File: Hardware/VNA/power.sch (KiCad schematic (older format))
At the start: 40 parts, among them Q1 RE1C002UN, U4 LP5912, U5 LP5912, U6 MIC5366-1.8

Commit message: first day of layout / routing done
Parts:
- F1: footprint VNA_Footprints:Fuse_1206_3216Metric -> VNA_Footprints:Fuse_0805_2012Metric
- Q1: footprint Package_TO_SOT_SMD:SOT-89-3 -> Package_TO_SOT_SMD:SOT-416
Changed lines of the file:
@@
 	5150 3950 5150 3800
 Connection ~ 4950 3950
-Text Notes 4000 3550 0    100  ~ 6
+Text Notes 4000 3550 0    100  ~ 20
 1V8 LDO\n
 Wire Wire Line
@@
 	1    0    0    -1
 $EndComp
-Text Notes 1300 2150 0    100  ~ 6
+Text Notes 1300 2150 0    100  ~ 20
 5V (Filtered)
-Text HLabel 3350 3800 1    49   Input ~ 6
+Text HLabel 3350 3800 1    49   Input ~ 10
 3V3A
-Text HLabel 5150 3800 1    49   Input ~ 6
+Text HLabel 5150 3800 1    49   Input ~ 10
 1V8
-Text HLabel 2550 2400 1    49   Input ~ 6
+Text HLabel 2550 2400 1    49   Input ~ 10
 5V0
 Wire Wire Line
@@
 	1    0    0    -1
 $EndComp
-Text Notes 2250 3600 2    100  ~ 6
+Text Notes 2250 3600 2    100  ~ 20
 3V3A LDO
 Wire Wire Line
@@
 Wire Wire Line
 	2550 3950 2850 3950
-Text HLabel 2850 3850 1    49   Input ~ 6
+Text HLabel 2850 3850 1    49   Input ~ 10
 3V3A
 Connection ~ 2550 3950
@@
 Wire Wire Line
 	4950 2500 5250 2500
-Text HLabel 5250 2400 1    49   Input ~ 6
+Text HLabel 5250 2400 1    49   Input ~ 10
 3V3
 Connection ~ 4950 2500
@@
 $EndComp
 Connection ~ 3750 2500
-Text Notes 4600 2200 2    100  ~ 6
+Text Notes 4600 2200 2    100  ~ 20
 3V3 LDO
 $Comp
@@
 F 0 "F1" V 1700 1400 50  0000 C CNN
 F 1 "500mA Polyfuse" V 1900 1400 50  0000 C CNN
-F 2 "VNA_Footprints:Fuse_1206_3216Metric" H 1850 1200 50  0001 L CNN
+F 2 "VNA_Footprints:Fuse_0805_2012Metric" H 1850 1200 50  0001 L CNN
 F 3 "~" H 1800 1400 50  0001 C CNN
 	1    1800 1400
 	0    1    1    0
 $EndComp
-Text HLabel 1250 1400 0    49   Input ~ 6
+Text HLabel 1250 1400 0    49   Input ~ 10
 VBUS
 Wire Wire Line
 	1900 1400 2200 1400
-Text Label 2300 1400 0    50   ~ 6
+Text Label 2300 1400 0    50   ~ 10
 VIN
-Text Label 1050 2400 1    50   ~ 6
+Text Label 1050 2400 1    50   ~ 10
 VIN
-Text Label 3350 2400 1    50   ~ 6
+Text Label 3350 2400 1    50   ~ 10
 VIN
-Text Label 1100 3850 1    50   ~ 6
+Text Label 1100 3850 1    50   ~ 10
 VIN
-Text Notes 1200 1150 0    100  ~ 6
+Text Notes 1200 1150 0    100  ~ 20
 Input Protection
 Wire Wire Line
@@
 F 0 "Q1" H 6706 3546 50  0000 L CNN
 F 1 "RE1C002UN" H 6706 3455 50  0000 L CNN
-F 2 "Package_TO_SOT_SMD:SOT-89-3" H 6700 3600 50  0001 C CNN
+F 2 "Package_TO_SOT_SMD:SOT-416" H 6700 3600 50  0001 C CNN
 F 3 "~" H 6500 3500 50  0001 C CNN
 	1    6500 3500
@@
 Wire Wire Line
 	6600 2600 6600 2550
-Text HLabel 6600 2550 1    50   Input ~ 6
+Text HLabel 6600 2550 1    50   Input ~ 10
 3V3A
-Text HLabel 6150 3500 0    50   Input ~ 6
+Text HLabel 6150 3500 0    50   Input ~ 10
 1V8
 Wire Wire Line
@@
 	1    0    0    -1
 $EndComp
-Text Notes 6800 2200 0    100  ~ 6
+Text Notes 6800 2200 0    100  ~ 20
 Voltage Rail LEDs
 Wire Wire Line
 	7250 2600 7250 2550
-Text HLabel 7250 2550 1    50   Input ~ 6
+Text HLabel 7250 2550 1    50   Input ~ 10
 3V3A
 Wire Wire Line
@@
 Wire Wire Line
 	7650 2600 7650 2550
-Text HLabel 7650 2550 1    50   Input ~ 6
+Text HLabel 7650 2550 1    50   Input ~ 10
 3V3
 Wire Wire Line
@@
 Wire Wire Line
 	8050 2600 8050 2550
-Text HLabel 8050 2550 1    50   Input ~ 6
+Text HLabel 8050 2550 1    50   Input ~ 10
 5V0
 Wire Wire Line
@@
 	1    0    0    -1
 $EndComp
-Text HLabel 8400 2550 1    49   Input ~ 6
+Text HLabel 8400 2550 1    49   Input ~ 10
 VBUS
 Connection ~ 5150 3950
@@
 	1    0    0    -1
 $EndComp
-Text Notes 9150 2200 0    100  ~ 6
+Text Notes 9150 2200 0    100  ~ 20
 Ground Test Points
 $Comp

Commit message: no unrouted nets!
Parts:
- Q1: footprint Package_TO_SOT_SMD:SOT-416 -> VNA_Footprints:SOT-416
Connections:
- net GND: no longer U5.3 (PG)
- no-connect marks 1 -> 2
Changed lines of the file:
@@
 $EndComp
-Wire Wire Line
-	4550 2700 4600 2700
-Wire Wire Line
-	4600 2700 4600 2800
 Wire Wire Line
 	4550 3000 4600 3000
@@
 Wire Wire Line
 	4550 2800 4600 2800
-Connection ~ 4600 2800
 Wire Wire Line
 	4600 2800 4600 2900
@@
 F 0 "Q1" H 6706 3546 50  0000 L CNN
 F 1 "RE1C002UN" H 6706 3455 50  0000 L CNN
-F 2 "Package_TO_SOT_SMD:SOT-416" H 6700 3600 50  0001 C CNN
+F 2 "VNA_Footprints:SOT-416" H 6700 3600 50  0001 C CNN
 F 3 "~" H 6500 3500 50  0001 C CNN
 	1    6500 3500
@@
 Wire Wire Line
 	3750 2500 3950 2500
+NoConn ~ 4550 2700
 $EndSCHEMATC

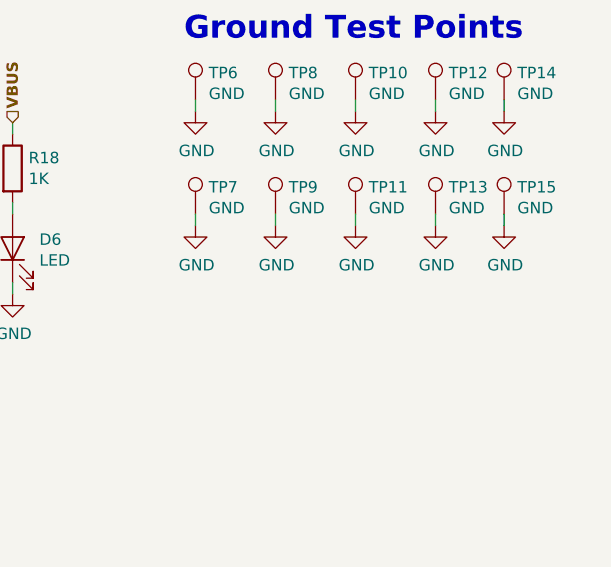
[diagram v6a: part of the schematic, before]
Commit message: Layout done, front and rear panels designed
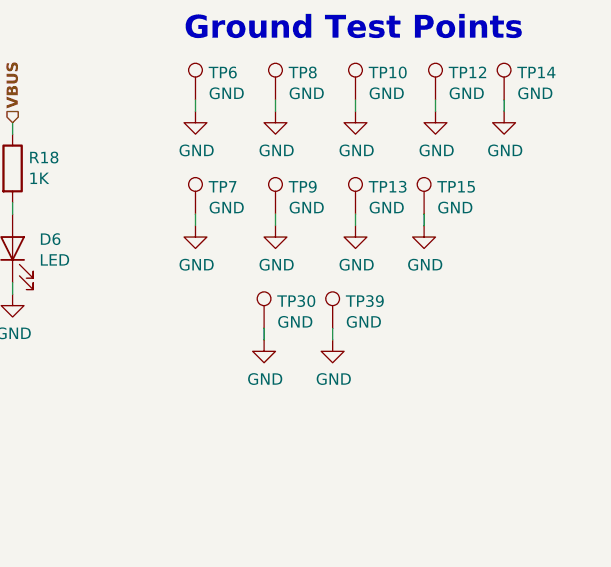
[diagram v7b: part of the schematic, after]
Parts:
- removed TP11: GND, VNA_Footprints:S1751-46_smdTestPoint, symbol Connector:TestPoint
- added TP30, TP39: GND, TestPoint:TestPoint_THTPad_D2.0mm_Drill1.0mm, symbol Connector:TestPoint
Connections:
- net GND: now also TP30.1, TP39.1
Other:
- moved on the sheet: TP13, TP15
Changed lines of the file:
@@
 $EndComp
 $Comp
-L Connector:TestPoint TP11
-U 1 1 5D0E22BA
+L Connector:TestPoint TP13
+U 1 1 5D0E4C7A
 P 9900 2950
-F 0 "TP11" H 9958 3068 50  0000 L CNN
+F 0 "TP13" H 9958 3068 50  0000 L CNN
 F 1 "GND" H 9958 2977 50  0000 L CNN
 F 2 "VNA_Footprints:S1751-46_smdTestPoint" H 10100 2950 50  0001 C CNN
@@
 $Comp
 L power:GND #PWR?
-U 1 1 5D0E22C1
+U 1 1 5D0E4C81
 P 9900 3000
-AR Path="/5CAA2138/5D0E22C1" Ref="#PWR?"  Part="1"
-AR Path="/5CA96610/5D0E22C1" Ref="#PWR050"  Part="1"
-F 0 "#PWR050" H 9900 2750 50  0001 C CNN
+AR Path="/5CAA2138/5D0E4C81" Ref="#PWR?"  Part="1"
+AR Path="/5CA96610/5D0E4C81" Ref="#PWR052"  Part="1"
+F 0 "#PWR052" H 9900 2750 50  0001 C CNN
 F 1 "GND" H 9905 2827 50  0000 C CNN
 F 2 "" H 9900 3000 50  0001 C CNN
@@
 $EndComp
 $Comp
-L Connector:TestPoint TP13
-U 1 1 5D0E4C7A
-P 10250 2950
-F 0 "TP13" H 10308 3068 50  0000 L CNN
-F 1 "GND" H 10308 2977 50  0000 L CNN
-F 2 "VNA_Footprints:S1751-46_smdTestPoint" H 10450 2950 50  0001 C CNN
-F 3 "~" H 10450 2950 50  0001 C CNN
-	1    10250 2950
-	1    0    0    -1
-$EndComp
-Wire Wire Line
-	10250 2950 10250 3000
-$Comp
-L power:GND #PWR?
-U 1 1 5D0E4C81
-P 10250 3000
-AR Path="/5CAA2138/5D0E4C81" Ref="#PWR?"  Part="1"
-AR Path="/5CA96610/5D0E4C81" Ref="#PWR052"  Part="1"
-F 0 "#PWR052" H 10250 2750 50  0001 C CNN
-F 1 "GND" H 10255 2827 50  0000 C CNN
-F 2 "" H 10250 3000 50  0001 C CNN
-F 3 "" H 10250 3000 50  0001 C CNN
-	1    10250 3000
-	1    0    0    -1
-$EndComp
-$Comp
 L Connector:TestPoint TP15
 U 1 1 5D0E7705
-P 10550 2950
-F 0 "TP15" H 10608 3068 50  0000 L CNN
-F 1 "GND" H 10608 2977 50  0000 L CNN
-F 2 "VNA_Footprints:S1751-46_smdTestPoint" H 10750 2950 50  0001 C CNN
-F 3 "~" H 10750 2950 50  0001 C CNN
-	1    10550 2950
-	1    0    0    -1
-$EndComp
-Wire Wire Line
-	10550 2950 10550 3000
+P 10200 2950
+F 0 "TP15" H 10258 3068 50  0000 L CNN
+F 1 "GND" H 10258 2977 50  0000 L CNN
+F 2 "VNA_Footprints:S1751-46_smdTestPoint" H 10400 2950 50  0001 C CNN
+F 3 "~" H 10400 2950 50  0001 C CNN
+	1    10200 2950
+	1    0    0    -1
+$EndComp
+Wire Wire Line
+	10200 2950 10200 3000
 $Comp
 L power:GND #PWR?
 U 1 1 5D0E770C
-P 10550 3000
+P 10200 3000
 AR Path="/5CAA2138/5D0E770C" Ref="#PWR?"  Part="1"
 AR Path="/5CA96610/5D0E770C" Ref="#PWR054"  Part="1"
-F 0 "#PWR054" H 10550 2750 50  0001 C CNN
-F 1 "GND" H 10555 2827 50  0000 C CNN
-F 2 "" H 10550 3000 50  0001 C CNN
-F 3 "" H 10550 3000 50  0001 C CNN
-	1    10550 3000
+F 0 "#PWR054" H 10200 2750 50  0001 C CNN
+F 1 "GND" H 10205 2827 50  0000 C CNN
+F 2 "" H 10200 3000 50  0001 C CNN
+F 3 "" H 10200 3000 50  0001 C CNN
+	1    10200 3000
 	1    0    0    -1
 $EndComp
@@
 	3750 2500 3950 2500
 NoConn ~ 4550 2700
+$Comp
+L Connector:TestPoint TP30
+U 1 1 5CBF524B
+P 9500 3450
+F 0 "TP30" H 9558 3568 50  0000 L CNN
+F 1 "GND" H 9558 3477 50  0000 L CNN
+F 2 "TestPoint:TestPoint_THTPad_D2.0mm_Drill1.0mm" H 9700 3450 50  0001 C CNN
+F 3 "~" H 9700 3450 50  0001 C CNN
+	1    9500 3450
+	1    0    0    -1
+$EndComp
+Wire Wire Line
+	9500 3450 9500 3500
+$Comp
+L power:GND #PWR?
+U 1 1 5CBF5252
+P 9500 3500
+AR Path="/5CAA2138/5CBF5252" Ref="#PWR?"  Part="1"
+AR Path="/5CA96610/5CBF5252" Ref="#PWR0127"  Part="1"
+F 0 "#PWR0127" H 9500 3250 50  0001 C CNN
+F 1 "GND" H 9505 3327 50  0000 C CNN
+F 2 "" H 9500 3500 50  0001 C CNN
+F 3 "" H 9500 3500 50  0001 C CNN
+	1    9500 3500
+	1    0    0    -1
+$EndComp
+$Comp
+L Connector:TestPoint TP39
+U 1 1 5CBF5258
+P 9800 3450
+F 0 "TP39" H 9858 3568 50  0000 L CNN
+F 1 "GND" H 9858 3477 50  0000 L CNN
+F 2 "TestPoint:TestPoint_THTPad_D2.0mm_Drill1.0mm" H 10000 3450 50  0001 C CNN
+F 3 "~" H 10000 3450 50  0001 C CNN
+	1    9800 3450
+	1    0    0    -1
+$EndComp
+Wire Wire Line
+	9800 3450 9800 3500
+$Comp
+L power:GND #PWR?
+U 1 1 5CBF525F
+P 9800 3500
+AR Path="/5CAA2138/5CBF525F" Ref="#PWR?"  Part="1"
+AR Path="/5CA96610/5CBF525F" Ref="#PWR0128"  Part="1"
+F 0 "#PWR0128" H 9800 3250 50  0001 C CNN
+F 1 "GND" H 9805 3327 50  0000 C CNN
+F 2 "" H 9800 3500 50  0001 C CNN
+F 3 "" H 9800 3500 50  0001 C CNN
+	1    9800 3500
+	1    0    0    -1
+$EndComp
 $EndSCHEMATC

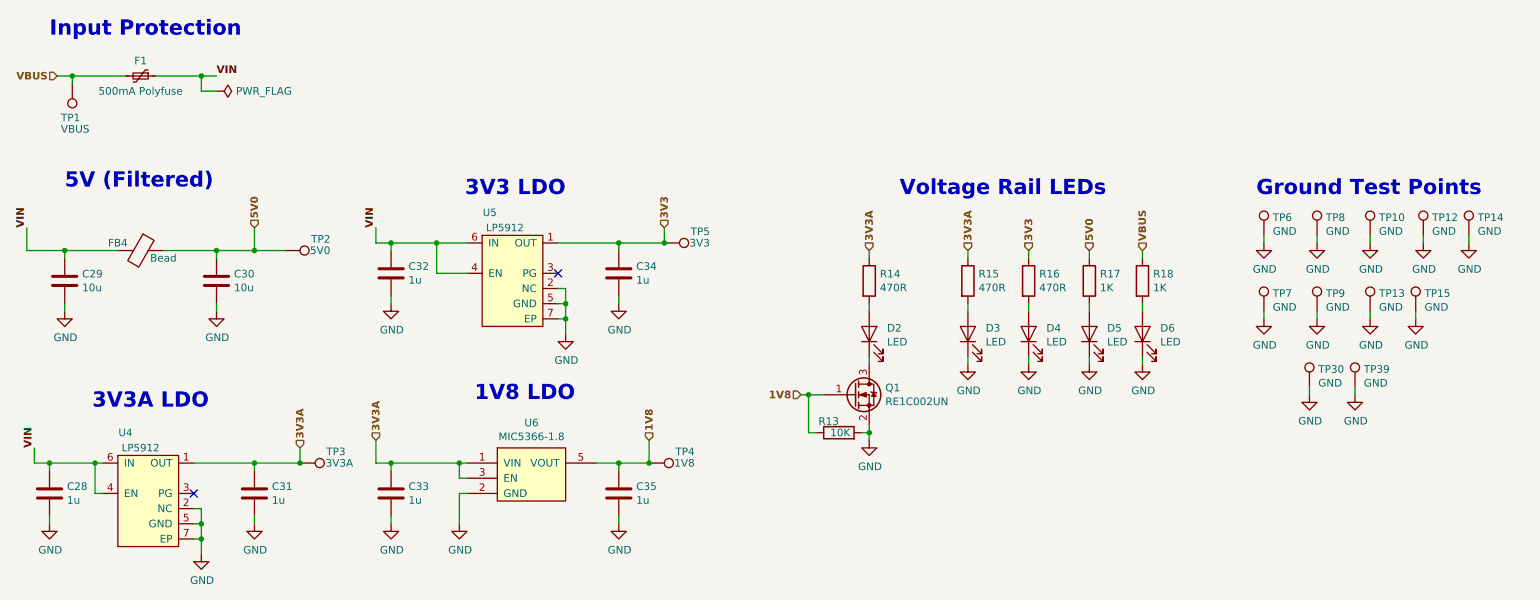
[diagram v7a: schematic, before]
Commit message: fix KiCad 5.1.0 bold after plot issue on schematics
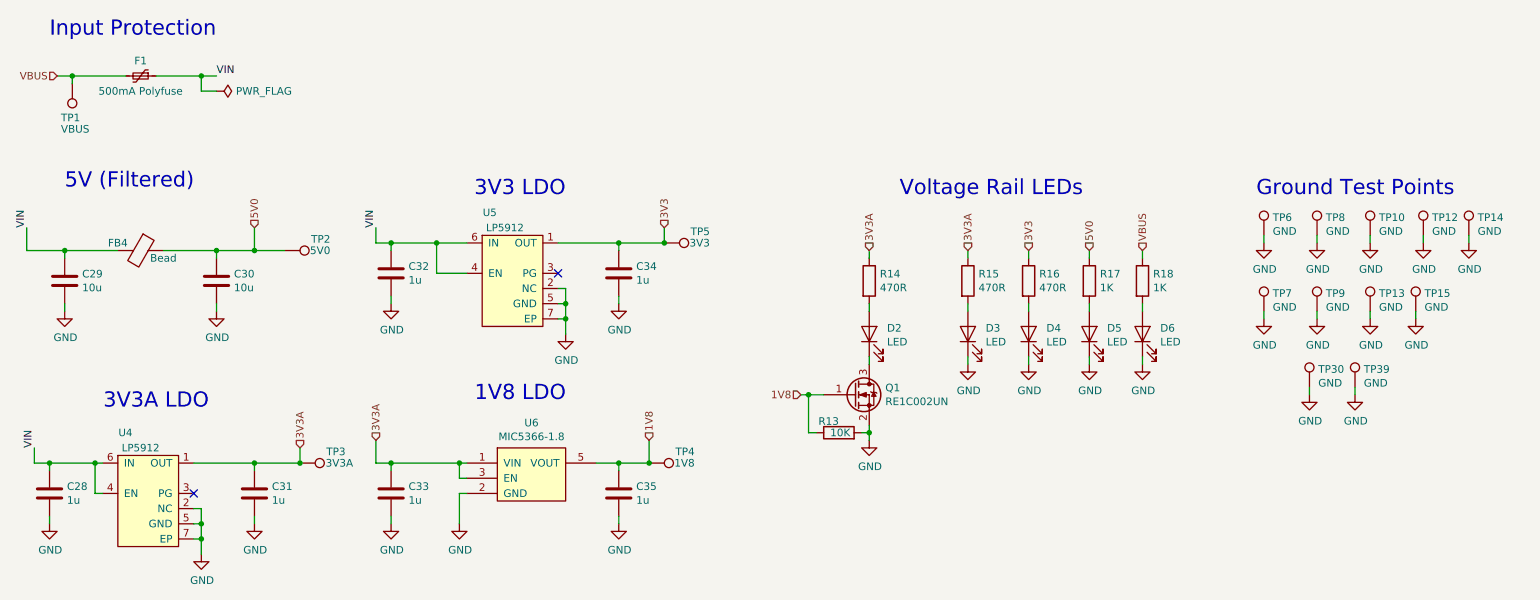
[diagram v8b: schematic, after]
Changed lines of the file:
@@
 	5150 3950 5150 3800
 Connection ~ 4950 3950
-Text Notes 4000 3550 0    100  ~ 20
+Text Notes 4000 3550 0    100  ~ 0
 1V8 LDO\n
 Wire Wire Line
@@
 	1    0    0    -1
 $EndComp
-Text Notes 1300 2150 0    100  ~ 20
+Text Notes 1300 2150 0    100  ~ 0
 5V (Filtered)
-Text HLabel 3350 3800 1    49   Input ~ 10
+Text HLabel 3350 3800 1    49   Input ~ 0
 3V3A
-Text HLabel 5150 3800 1    49   Input ~ 10
+Text HLabel 5150 3800 1    49   Input ~ 0
 1V8
-Text HLabel 2550 2400 1    49   Input ~ 10
+Text HLabel 2550 2400 1    49   Input ~ 0
 5V0
 Wire Wire Line
@@
 	1    0    0    -1
 $EndComp
-Text Notes 2250 3600 2    100  ~ 20
+Text Notes 2250 3600 2    100  ~ 0
 3V3A LDO
 Wire Wire Line
@@
 Wire Wire Line
 	2550 3950 2850 3950
-Text HLabel 2850 3850 1    49   Input ~ 10
+Text HLabel 2850 3850 1    49   Input ~ 0
 3V3A
 Connection ~ 2550 3950
@@
 Wire Wire Line
 	4950 2500 5250 2500
-Text HLabel 5250 2400 1    49   Input ~ 10
+Text HLabel 5250 2400 1    49   Input ~ 0
 3V3
 Connection ~ 4950 2500
@@
 $EndComp
 Connection ~ 3750 2500
-Text Notes 4600 2200 2    100  ~ 20
+Text Notes 4600 2200 2    100  ~ 0
 3V3 LDO
 $Comp
@@
 	0    1    1    0
 $EndComp
-Text HLabel 1250 1400 0    49   Input ~ 10
+Text HLabel 1250 1400 0    49   Input ~ 0
 VBUS
 Wire Wire Line
 	1900 1400 2200 1400
-Text Label 2300 1400 0    50   ~ 10
+Text Label 2300 1400 0    50   ~ 0
 VIN
-Text Label 1050 2400 1    50   ~ 10
+Text Label 1050 2400 1    50   ~ 0
 VIN
-Text Label 3350 2400 1    50   ~ 10
+Text Label 3350 2400 1    50   ~ 0
 VIN
-Text Label 1100 3850 1    50   ~ 10
+Text Label 1100 3850 1    50   ~ 0
 VIN
-Text Notes 1200 1150 0    100  ~ 20
+Text Notes 1200 1150 0    100  ~ 0
 Input Protection
 Wire Wire Line
@@
 Wire Wire Line
 	6600 2600 6600 2550
-Text HLabel 6600 2550 1    50   Input ~ 10
+Text HLabel 6600 2550 1    50   Input ~ 0
 3V3A
-Text HLabel 6150 3500 0    50   Input ~ 10
+Text HLabel 6150 3500 0    50   Input ~ 0
 1V8
 Wire Wire Line
@@
 	1    0    0    -1
 $EndComp
-Text Notes 6800 2200 0    100  ~ 20
+Text Notes 6800 2200 0    100  ~ 0
 Voltage Rail LEDs
 Wire Wire Line
 	7250 2600 7250 2550
-Text HLabel 7250 2550 1    50   Input ~ 10
+Text HLabel 7250 2550 1    50   Input ~ 0
 3V3A
 Wire Wire Line
@@
 Wire Wire Line
 	7650 2600 7650 2550
-Text HLabel 7650 2550 1    50   Input ~ 10
+Text HLabel 7650 2550 1    50   Input ~ 0
 3V3
 Wire Wire Line
@@
 Wire Wire Line
 	8050 2600 8050 2550
-Text HLabel 8050 2550 1    50   Input ~ 10
+Text HLabel 8050 2550 1    50   Input ~ 0
 5V0
 Wire Wire Line
@@
 	1    0    0    -1
 $EndComp
-Text HLabel 8400 2550 1    49   Input ~ 10
+Text HLabel 8400 2550 1    49   Input ~ 0
 VBUS
 Connection ~ 5150 3950
@@
 	1    0    0    -1
 $EndComp
-Text Notes 9150 2200 0    100  ~ 20
+Text Notes 9150 2200 0    100  ~ 0
 Ground Test Points
 $Comp
